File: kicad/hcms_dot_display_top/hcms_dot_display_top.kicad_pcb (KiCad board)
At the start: 4 copper layers, 35.6 x 19.8 mm, 27 parts, among them J1 Conn_01x12, J3 Conn_01x12, J4 Conn_01x11_Male, J6 Conn_01x12, J7 Conn_01x12, Q1 Q_PMOS_DSG, Q2 Q_PMOS_DSG, Q3 Q_PMOS_DSG, Q4 Q_PMOS_DSG, Q5 Q_PMOS_DSG

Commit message: edits to top
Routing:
- net /COL_4: track 15.7 -> 13.3 mm
- net /MCU_COL_5: track 67.1 -> 68.2 mm
- net /MCU_COL_2: track 70.8 -> 70.3 mm
- net GND: track 41.8 -> 41.5 mm, vias 3 -> 29

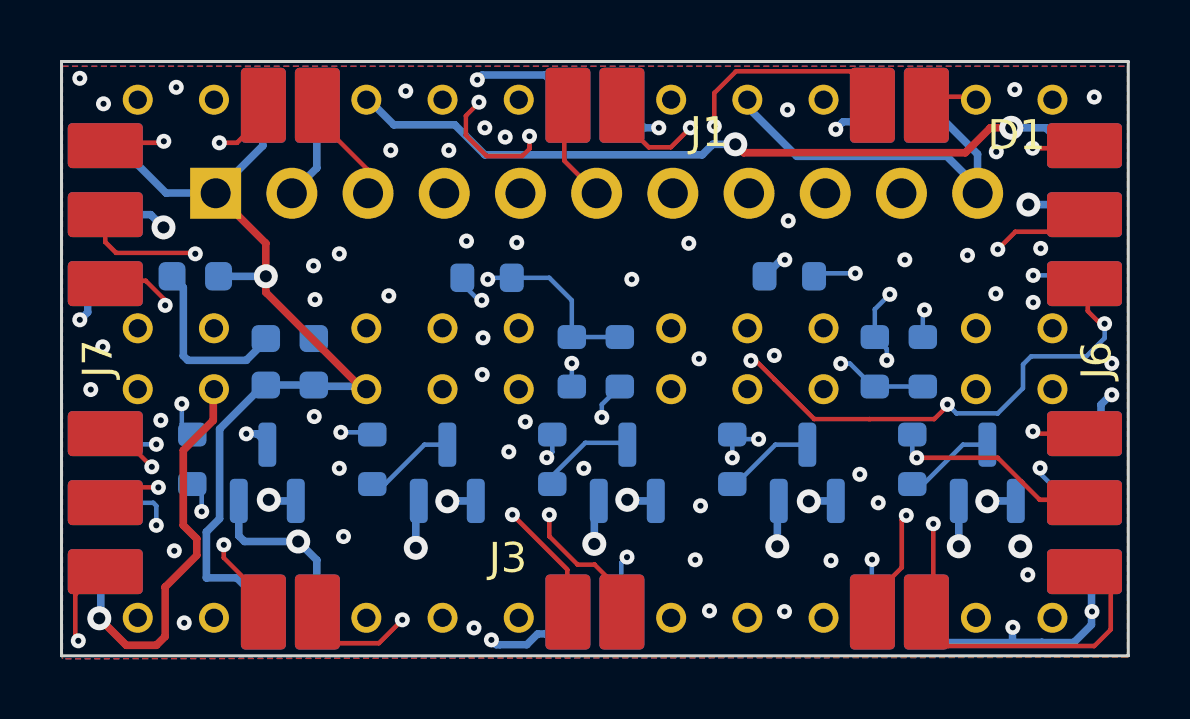
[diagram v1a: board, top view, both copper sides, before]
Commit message: Updated DMP footprint on bottom board and re routed
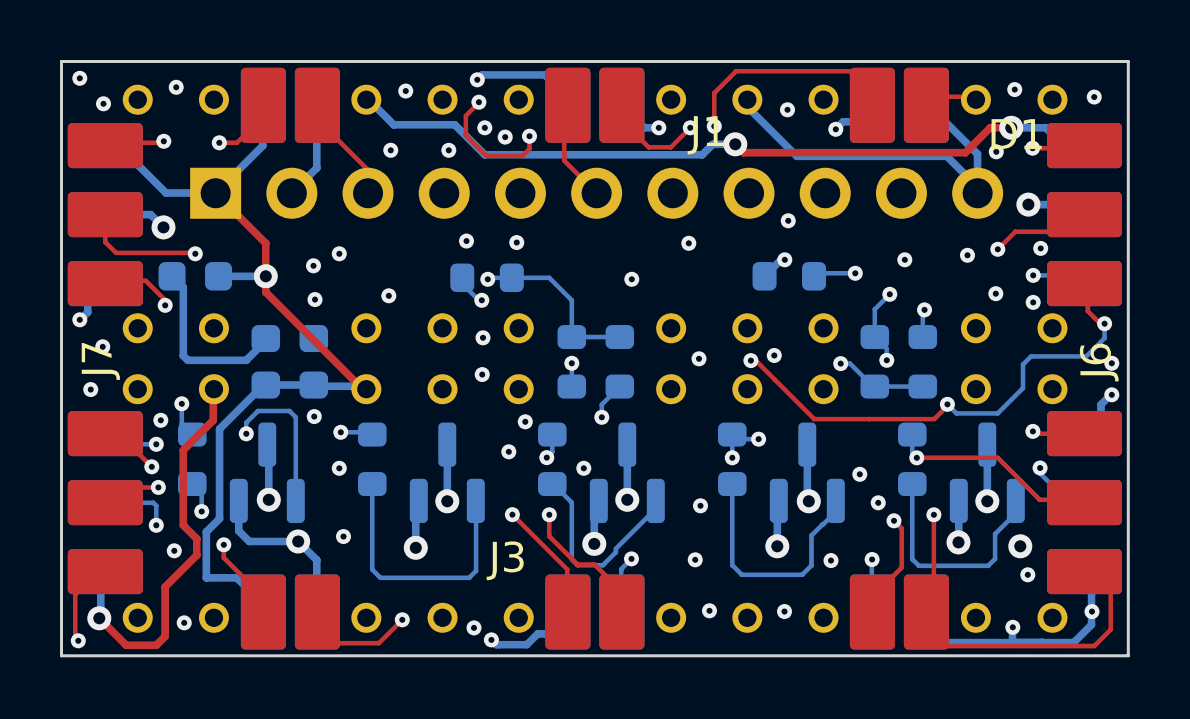
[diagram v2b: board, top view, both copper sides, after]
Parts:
- Q1, Q2, Q3, Q4, Q5: value Q_PMOS_DSG -> Q_PMOS_GSD
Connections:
- Q1 pad 1: /COL_1 -> Net-(Q1-Pad1)
- Q1 pad 3: Net-(Q1-Pad3) -> /COL_1
- Q2 pad 1: /COL_2 -> Net-(Q2-Pad1)
- Q2 pad 3: Net-(Q2-Pad3) -> /COL_2
- Q3 pad 1: /COL_3 -> Net-(Q3-Pad1)
- Q3 pad 3: Net-(Q3-Pad3) -> /COL_3
- Q4 pad 1: /COL_4 -> Net-(Q4-Pad1)
- Q4 pad 3: Net-(Q4-Pad3) -> /COL_4
- Q5 pad 1: /COL_5 -> Net-(Q5-Pad1)
- Q5 pad 3: Net-(Q5-Pad3) -> /COL_5
- R10 pad 1: Net-(Q1-Pad3) -> Net-(Q1-Pad1)
- R11 pad 1: Net-(Q2-Pad3) -> Net-(Q2-Pad1)
- R12 pad 1: Net-(Q3-Pad3) -> Net-(Q3-Pad1)
- R13 pad 1: Net-(Q4-Pad3) -> Net-(Q4-Pad1)
- R14 pad 1: Net-(Q5-Pad3) -> Net-(Q5-Pad1)
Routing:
- net Net-(Q2-Pad1): track 0.00 -> 9.32 mm, vias 0 -> 2
- net Net-(Q4-Pad1): track 0.00 -> 8.86 mm
- net Net-(Q3-Pad1): track 0.00 -> 8.11 mm
- net Net-(Q5-Pad1): track 0.00 -> 7.67 mm
- net Net-(Q1-Pad1): track 0.00 -> 6.79 mm
- net Net-(Q2-Pad3): track 5.13 -> 0.00 mm, vias 2 -> 0
- net Net-(Q1-Pad3): track 3.26 -> 0.00 mm
- net Net-(Q5-Pad3): track 3.04 -> 0.00 mm
- net Net-(Q4-Pad3): track 3.04 -> 0.00 mm
- net Net-(Q3-Pad3): track 3.04 -> 0.00 mm
- net /COL_3: track 11.4 -> 12.4 mm
- net /COL_2: track 13.8 -> 14.7 mm
- net /COL_5: track 11.2 -> 12.2 mm
- net /COL_4: track 13.3 -> 14.2 mm
- net /COL_1: track 12.2 -> 13.1 mm
